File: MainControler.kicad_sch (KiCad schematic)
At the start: 26 parts, among them J1 Conn_01x10_Pin, U18 ESP32-S3-DevKitC, U7 SX1509

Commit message: progress
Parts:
- renumbered C71 to C4, C57 to C5, C72 to C6, J1 to J2, R61 to R13, R62 to R14, R34 to R15, R26 to R16, R29 to R17, R58 to R18, R20 to R19, R19 to R20, R22 to R21, R30 to R22, R21 to R23, R23 to R24, R35 to R25, R24 to R26, R76 to R27, R25 to R28, R77 to R29, R27 to R30, R28 to R31, R78 to R32, U18 to U4, U7 to U5

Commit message: small changes
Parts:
- added J20, J21, J23, J24, J25: 1935161, SamacSys_Parts:1935161, symbol SamacSys_Parts:1935161
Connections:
- net GND: now also J20.2, J23.2, J24.1
- net IO_5: now reaches U5.16 (I/O[11])
- net IO_5: now also J21.1
- net IO_6: now reaches U5.19 (I/O[12])
- net IO_6: now also J21.2
- net IO_7: now reaches U5.20 (I/O[13])
- net IO_7: now also J23.1
- net IO_1: now reaches U5.5 (I/O[4])
- net IO_1: now also J24.2
- net IO_2: now reaches U5.6 (I/O[5])
- net IO_2: now also J25.1
- net IO_3: now reaches U5.7 (I/O[6])
- net IO_3: now also J25.2
- net IO_4: now reaches U5.8 (I/O[7])
- net IO_4: now also J20.1
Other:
- note added: "Extra IO"

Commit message: add mouser sch tooling
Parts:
- J2: Mouser (none) -> https://www.mouser.com/en/ProductDetail/JST-Commercial/B10B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
- U4: Mouser (none) -> https://www.mouser.com/en/ProductDetail/Espressif-Systems/E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
- U5: Manufacturer_Part_Number (none) -> SX1509BIULTRT; Mouser (none) -> https://www.mouser.com/en/ProductDetail/Semtech/SX1509BIULT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; PROD_ID IC-11311 -> (none)
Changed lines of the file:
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@@
+			)
+		)
+		(property "Mouser" "https://www.mouser.com/en/ProductDetail/Espressif-Systems/ESP32-S3-DevKitC-1U-N8R8?qs=Li%252BoUPsLEnv4qqHEsdK%252Bbw%3D%3D&mgh=1&srsltid=AfmBOoqOS62ebvUcmBEUILNpX5fCCt5DrE-3pTM-xdvtT0he9Jzm1cB1j68"
+			(at 133.35 101.6 0)
+			(hide yes)
+			(show_name no)
+			(do_not_autoplace no)
+			(effects
+				(font
+					(size 1.27 1.27)
+				)
 			)
 		)
@@
 			)
 		)
+		(property "Mouser" "https://www.mouser.com/en/ProductDetail/JST-Commercial/B10B-XH-AMLFSN?qs=cIziFXvMxOVgWRjUQes4Xw%3D%3D&srsltid=AfmBOork195JkJExIa92VuCwqISfS--gMCfu7LP7OFkak7bxlowy1x8f"
+			(at 366.776 51.054 0)
+			(hide yes)
+			(show_name no)
+			(do_not_autoplace no)
+			(effects
+				(font
+					(size 1.27 1.27)
+				)
+			)
+		)
 		(pin "5"
 		)
@@
 			)
 		)
-		(property "PROD_ID" "IC-11311"
+		(property "Mouser" "https://www.mouser.com/en/ProductDetail/Semtech/SX1509BIULTRT?qs=rBWM4%252BvDhIdubk63kOvGUA%3D%3D"
+			(at 251.714 259.842 0)
+			(hide yes)
+			(show_name no)
+			(do_not_autoplace no)
+			(effects
+				(font
+					(size 1.27 1.27)
+				)
+			)
+		)
+		(property "Manufacturer_Part_Number" "SX1509BIULTRT"
 			(at 249.428 264.414 0)
 			(hide yes)

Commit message: pcb update
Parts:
- added R104, R105: 390, Resistor_SMD:R_0402_1005Metric, symbol Device:R
- added R106: 2.2k, Resistor_SMD:R_0402_1005Metric, symbol Device:R
- added U13, U14: TCMT1109, Package_SO:SOP-4_4.4x2.6mm_P1.27mm, symbol Isolator:TCMT1109
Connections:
- net 3.3V_Main: now also R106.2
- net GND: now also U13.3, U14.2; no longer J20.2, J24.1
- net IO_1: now also R106.1, U13.4; no longer J24.2
- net IO_2: now also R105.1; no longer J25.1
- net IO_3: now also J20.1; no longer J25.2
- net IO_4: now also J20.2; no longer J20.1
- new net: R105.2, U14.1
- new net: J25.2, U14.3
- new net: J25.1, U14.4
- new net: J24.1, R104.1
- new net: J24.2, U13.2
- new net: R104.2, U13.1
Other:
- note added: "anything with an external power supply"
- note added: "should connect to the isolated io"
- note added: "to maintain ground isolation in this board"
- moved on the sheet: J20, J21, J23, J24, J25, R16, R17

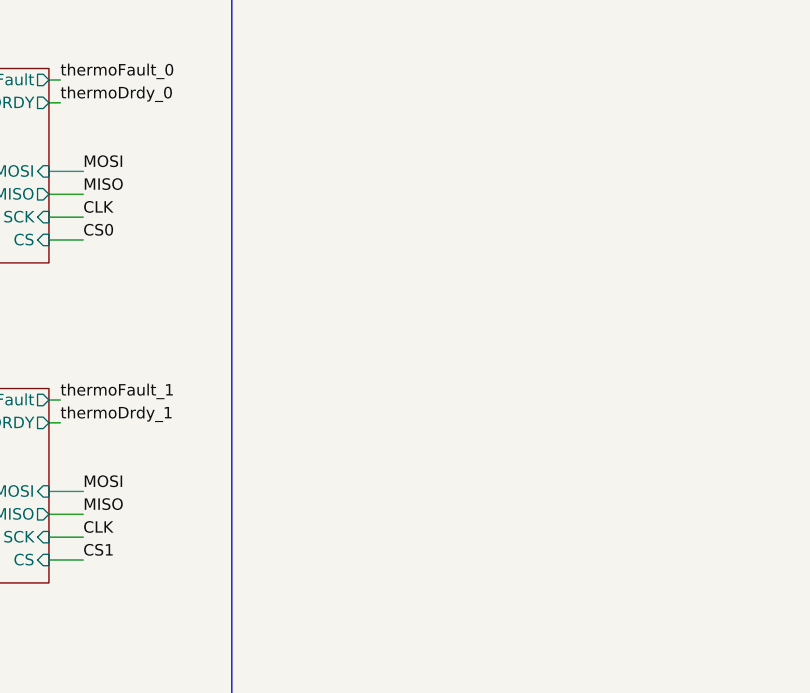
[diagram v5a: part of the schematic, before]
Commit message: start adding seprate Thermocouple Board, fix some errors
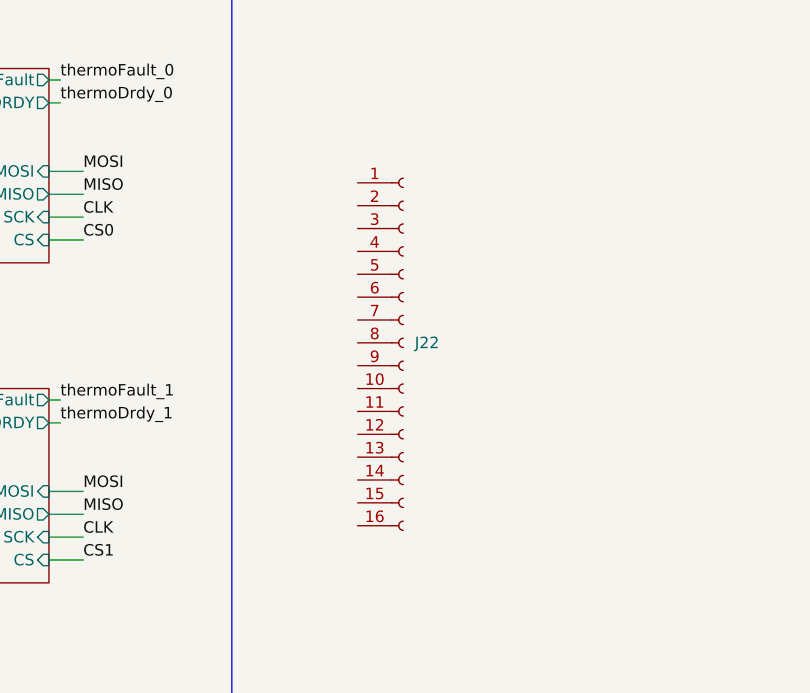
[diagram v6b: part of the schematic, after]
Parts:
- added J22: Conn_01x16_Socket, Connector_PinSocket_2.54mm:PinSocket_1x16_P2.54mm_Horizontal, symbol Connector:Conn_01x16_Socket
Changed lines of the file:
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@@
+	)
+	(symbol
+		(lib_id "Connector:Conn_01x16_Socket")
+		(at 109.22 152.4 0)
+		(unit 1)
+		(body_style 1)
+		(exclude_from_sim no)
+		(in_bom yes)
+		(on_board yes)
+		(in_pos_files yes)
+		(dnp no)
+		(fields_autoplaced yes)
+		(property "Reference" "J22"
+			(at 110.49 152.3999 0)
+			(show_name no)
+			(do_not_autoplace no)
+			(effects
+				(font
+					(size 1.27 1.27)
+				)
+				(justify left)
+			)
+		)
+		(property "Value" "Conn_01x16_Socket"
+			(at 110.49 154.9399 0)
+			(hide yes)
+			(show_name no)
+			(do_not_autoplace no)
+			(effects
+				(font
+					(size 1.27 1.27)
+				)
+				(justify left)
+			)
+		)
+		(property "Footprint" "Connector_PinSocket_2.54mm:PinSocket_1x16_P2.54mm_Horizontal"
+			(at 109.22 152.4 0)
+			(hide yes)
+			(show_name no)
+			(do_not_autoplace no)
+			(effects
+				(font
+					(size 1.27 1.27)
+				)
+			)
+		)
+		(property "Datasheet" ""
+			(at 109.22 152.4 0)
+			(hide yes)
+			(show_name no)
+			(do_not_autoplace no)
+			(effects
+				(font
+					(size 1.27 1.27)
+				)
+			)
+		)
+		(property "Mouser Part Number Alt" "https://www.mouser.com/en/ProductDetail/Preci-dip/801-87-016-20-001101?qs=q5BRkYolQ3h9IaexLLDn4Q%3D%3D"
+			(at 109.22 152.4 0)
+			(hide yes)
+			(show_name no)
+			(do_not_autoplace no)
+			(effects
+				(font
+					(size 1.27 1.27)
+				)
+			)
+		)
+		(property "Mouser" "https://www.mouser.com/en/ProductDetail/Preci-dip/801-83-016-20-001101?qs=q5BRkYolQ3gVVxr%252BmS6fPA%3D%3D"
+			(at 109.22 152.4 0)
+			(hide yes)
+			(show_name no)
+			(do_not_autoplace no)
+			(effects
+				(font
+					(size 1.27 1.27)
+				)
+			)
+		)
+		(property "Description" "Generic connector, single row, 01x16, script generated"
+			(at 109.22 152.4 0)
+			(hide yes)
+			(show_name no)
+			(do_not_autoplace no)
+			(effects
+				(font
+					(size 1.27 1.27)
+				)
+			)
+		)
+		(pin "2"
+		)
+		(pin "4"
+		)
+		(pin "6"
+		)
+		(pin "8"
+		)
+		(pin "11"
+		)
+		(pin "14"
+		)
+		(pin "1"
+		)
+		(pin "3"
+		)
+		(pin "5"
+		)
+		(pin "7"
+		)
+		(pin "9"
+		)
+		(pin "10"
+		)
+		(pin "12"
+		)
+		(pin "13"
+		)
+		(pin "15"
+		)
+		(pin "16"
+		)
+		(instances
+			(project "kiln"
+				(path "/e9c1836b-d16f-494a-819b-41549a786e18/307f7e78-c7c7-4c1f-bfd5-4e5fce95f524"
+					(reference "J22")
+					(unit 1)
+				)
+			)
+		)
 	)
 	(symbol
